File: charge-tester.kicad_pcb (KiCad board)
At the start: 2 copper layers, 85 x 56 mm, 76 parts, among them J1 Conn_01x02, J2 Conn_01x02, J3 Conn_01x02, J4 Conn_01x02, J5 Conn_01x06, Q1 IRFB4020, Q2 FDV303N, Q3 FDV303N, SW1 SW_Push, U1 TPS7B88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

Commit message: pcb: Improve silkscreen
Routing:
- net GND: vias 196 -> 221
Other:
- board text added: "CAN CHARGER"
- board text removed: "12S CAN CHARGER"

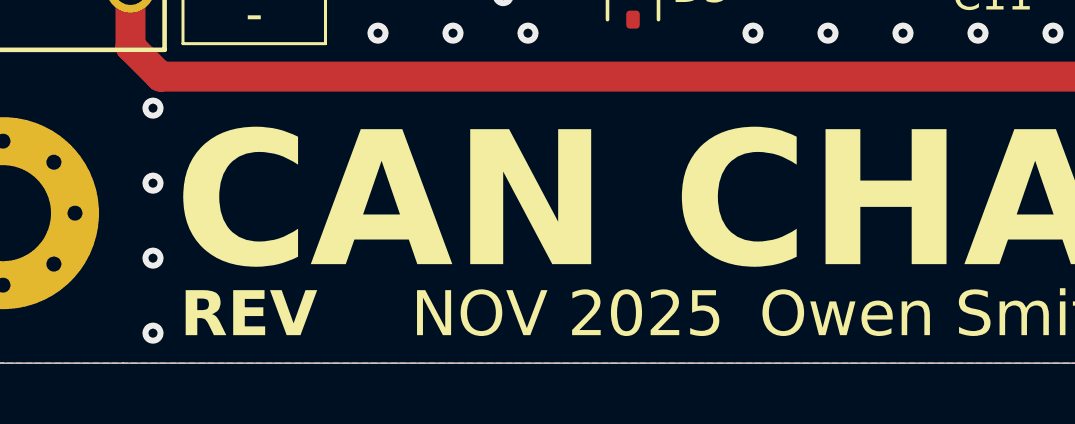
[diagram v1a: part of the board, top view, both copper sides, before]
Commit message: *: Fill in info boxes
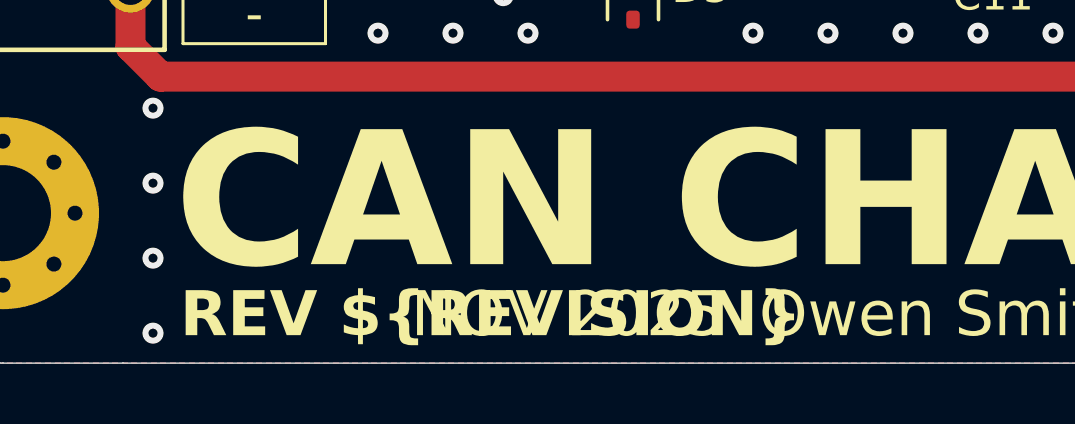
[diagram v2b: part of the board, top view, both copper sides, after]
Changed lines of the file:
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@@
 	)
 	(paper "A4")
+	(title_block
+		(title "Linear Battery Charger")
+		(date "2025-11-22")
+		(rev "${REVISION}")
+		(company "York Formula Student")
+	)
 	(layers
 		(0 "F.Cu" signal)

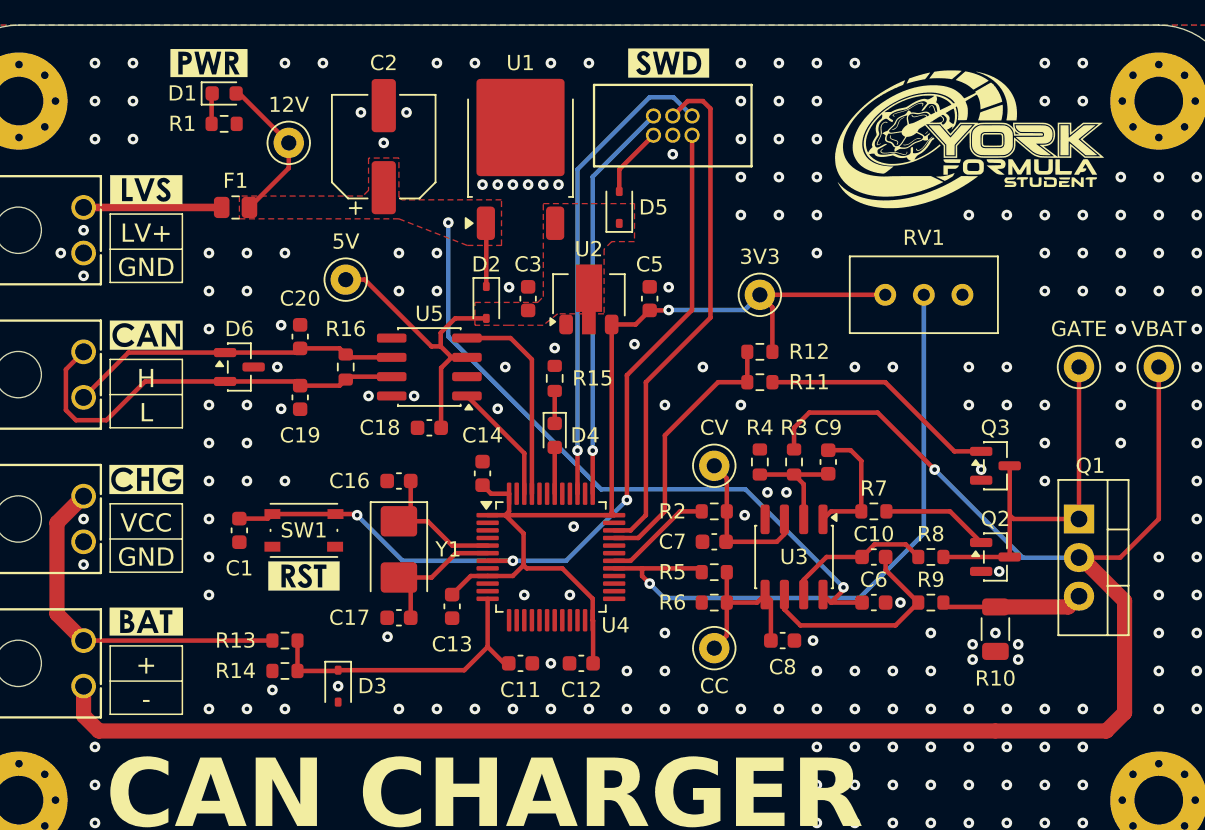
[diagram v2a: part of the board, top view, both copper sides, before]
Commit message: pcb: Run cleanup tracks
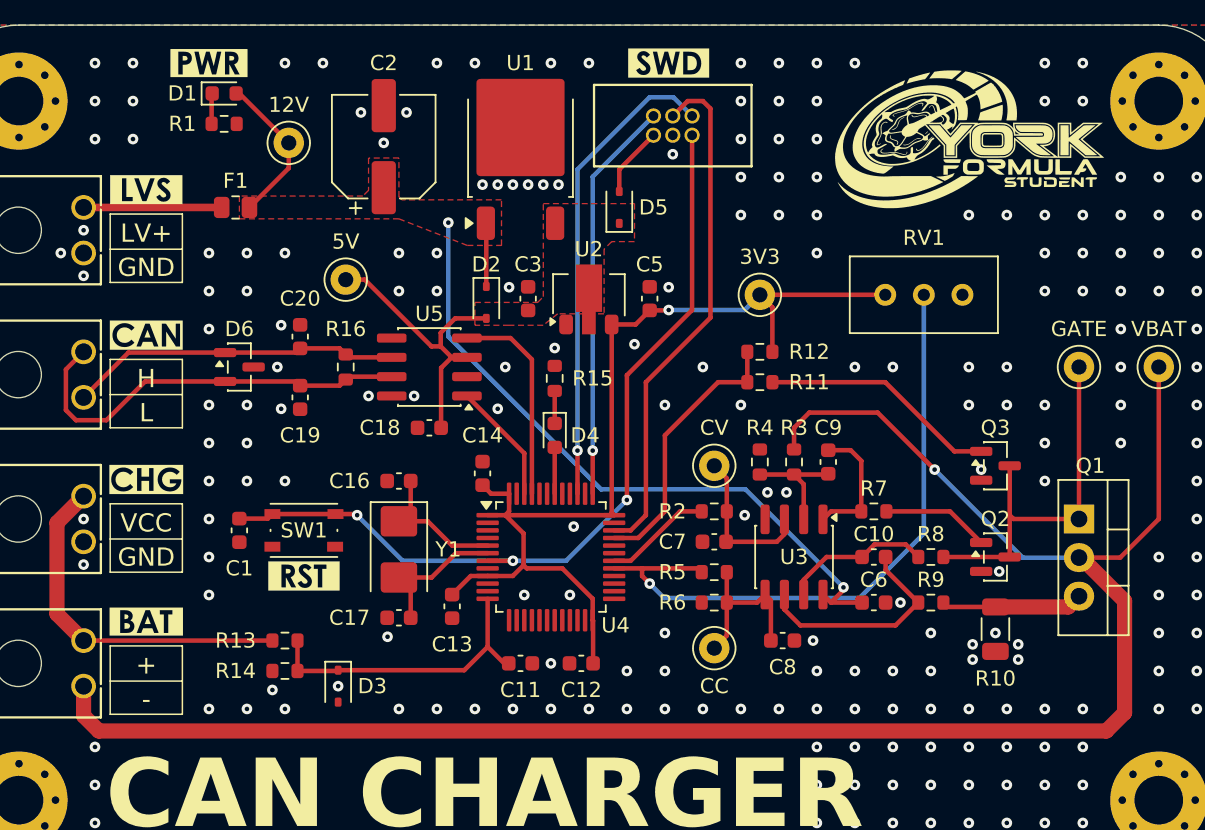
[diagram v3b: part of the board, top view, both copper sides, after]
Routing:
- net /HSE_OUT: track 9.47 -> 8.38 mm
- net /HSE_IN: track 9.47 -> 8.38 mm
- net CANL: track 21.9 -> 21.2 mm
- net CANH: track 27.4 -> 26.8 mm
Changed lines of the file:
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@@
 	)
 	(segment
-		(start 89.5 34.5)
-		(end 89.2875 34.5)
-		(width 0.3)
-		(layer "F.Cu")
-		(net 1)
-	)
-	(segment
 		(start 92.75 37.75)
 		(end 89.5 34.5)
@@
 	)
 	(segment
-		(start 105.75 43.07)
-		(end 105.72 43.04)
-		(width 0.3)
-		(layer "F.Cu")
-		(net 1)
-	)
-	(segment
 		(start 105.75 47.2)
 		(end 105.75 43.07)
@@
 	)
 	(segment
-		(start 121.575 63.95)
-		(end 121.525 64)
-		(width 0.3)
-		(layer "F.Cu")
-		(net 5)
-	)
-	(segment
 		(start 121.575 59.825)
 		(end 120.75 59)
@@
 	)
 	(segment
-		(start 128.2 59.575)
-		(end 128.25 59.525)
-		(width 0.3)
-		(layer "F.Cu")
-		(net 8)
-	)
-	(segment
 		(start 123.75 59.575)
 		(end 126 59.575)
@@
 	)
 	(segment
-		(start 95.95 72.5)
-		(end 96 72.45)
-		(width 0.3)
-		(layer "F.Cu")
-		(net 11)
-	)
-	(segment
 		(start 105.8375 70.9125)
 		(end 105.8375 67.75)
@@
 	)
 	(segment
-		(start 107.225 72)
-		(end 106.925 72)
-		(width 0.3)
-		(layer "F.Cu")
-		(net 11)
-	)
-	(segment
 		(start 105.8375 64.25)
 		(end 103.5 64.25)
@@
 	)
 	(segment
-		(start 100.775 61.875)
-		(end 100 62.65)
-		(width 0.3)
-		(layer "F.Cu")
-		(net 12)
-	)
-	(segment
 		(start 103.5 64.25)
 		(end 101.9 62.65)
@@
 	)
 	(segment
-		(start 100.775 67.125)
-		(end 100 66.35)
-		(width 0.3)
-		(layer "F.Cu")
-		(net 13)
-	)
-	(segment
 		(start 102.15 66.35)
 		(end 100 66.35)
@@
 	)
 	(segment
-		(start 93.225 53.45)
-		(end 93.5 53.725)
-		(width 0.3)
-		(layer "F.Cu")
-		(net 14)
-	)
-	(segment
-		(start 96.69 53.135)
-		(end 96.5 53.325)
-		(width 0.3)
-		(layer "F.Cu")
-		(net 14)
-	)
-	(segment
 		(start 99.525 53.135)
 		(end 96.69 53.135)
@@
 	)
 	(segment
-		(start 96.69 51.865)
-		(end 96.5 51.675)
-		(width 0.3)
-		(layer "F.Cu")
-		(net 15)
-	)
-	(segment
-		(start 93.225 51.55)
-		(end 93.5 51.275)
-		(width 0.3)
-		(layer "F.Cu")
-		(net 15)
-	)
-	(segment
 		(start 99.525 51.865)
 		(end 96.69 51.865)
@@
 	)
 	(segment
-		(start 87.675 34.5375)
-		(end 87.7125 34.5)
-		(width 0.3)
-		(layer "F.Cu")
-		(net 16)
-	)
-	(segment
 		(start 110.25 60.8375)
 		(end 110.25 57.7875)
@@
 	)
 	(segment
-		(start 139.301 76.449)
-		(end 146.551 76.449)
-		(width 1)
-		(layer "F.Cu")
-		(net 22)
-	)
-	(segment
 		(start 147.75 75.25)
 		(end 147.75 67.895)
@@
 	)
 	(segment
-		(start 144.71 65)
-		(end 144.75 65.04)
-		(width 0.3)
-		(layer "F.Cu")
-		(net 22)
-	)
-	(segment
 		(start 146.551 76.449)
 		(end 147.75 75.25)
@@
 	)
 	(segment
-		(start 144.895 65.04)
-		(end 144.75 65.04)
-		(width 1)
-		(layer "F.Cu")
-		(net 22)
-	)
-	(segment
 		(start 135.25 59.25)
 		(end 131.5 55.5)
@@
 	(segment
 		(start 80.25 76.449)
-		(end 139.199 76.449)
+		(end 146.551 76.449)
 		(width 1)
 		(layer "F.Cu")
@@
 		(width 0.3)
 		(layer "F.Cu")
-		(net 32)
-	)
-	(segment
-		(start 119.675 65.75)
-		(end 119.925 66)
-		(width 0.3)
-		(layer "F.Cu")
